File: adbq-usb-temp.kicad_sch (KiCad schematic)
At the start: 0 parts

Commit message: schem: add ESP32-S3FH4R2 symbol
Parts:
- added U1: ESP32-S3FH4R2, Package_DFN_QFN:QFN-56-1EP_7x7mm_P0.4mm_EP5.6x5.6mm, symbol PCM_Espressif:ESP32-S3
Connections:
- new net: U1.55 (VDDA), U1.56 (VDDA)
- new net GND: U1.57 (GND)
- new net VDD3P3: U1.2 (VDD3P3), U1.3 (VDD3P3)

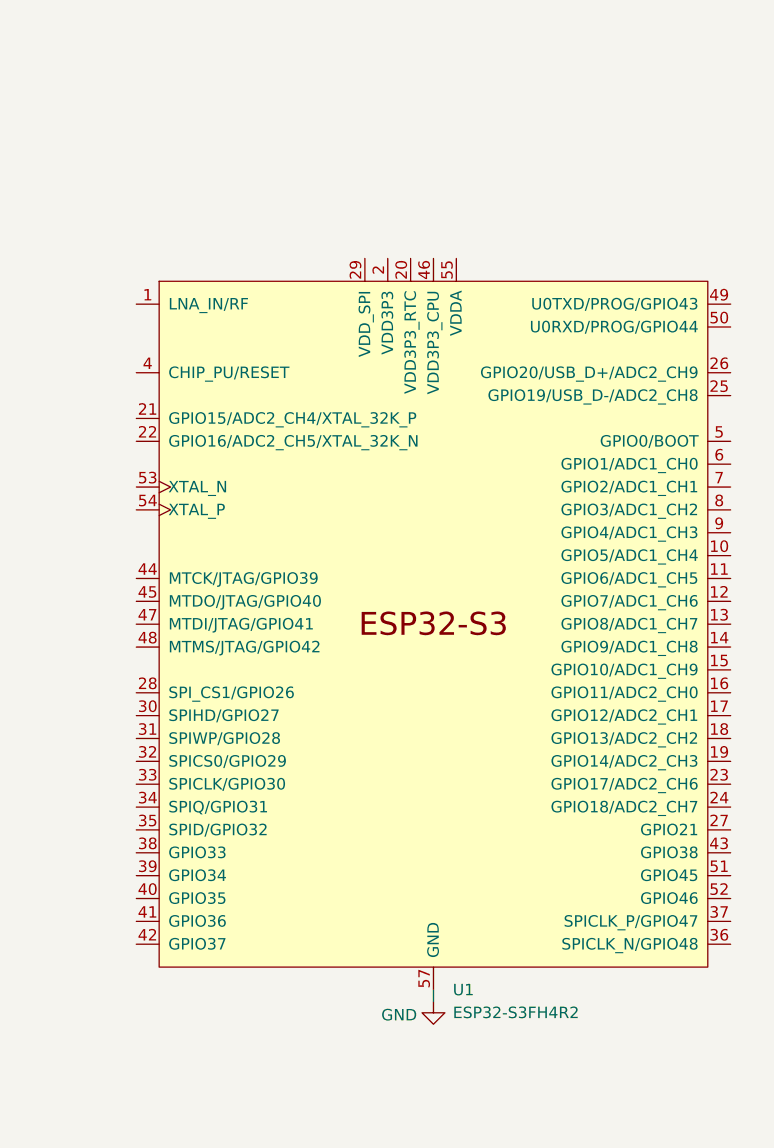
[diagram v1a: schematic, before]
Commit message: schem: add ESP32 decoupling caps
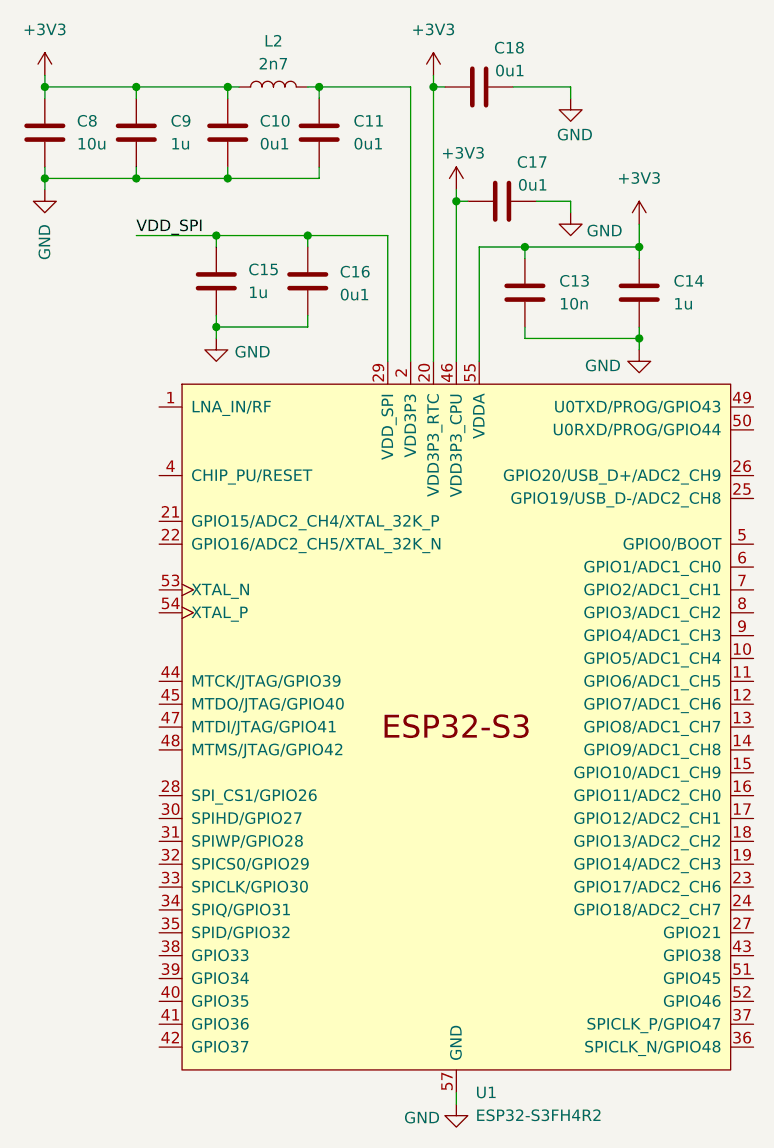
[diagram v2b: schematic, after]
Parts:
- added C10, C11, C16, C17, C18: 0u1, Capacitor_SMD:C_0402_1005Metric, symbol Device:C
- added C13: 10n, Capacitor_SMD:C_0402_1005Metric, symbol Device:C
- added C14, C15, C9: 1u, Capacitor_SMD:C_0402_1005Metric, symbol Device:C
- added C8: 10u, Capacitor_SMD:C_0402_1005Metric, symbol Device:C
- added L2: 2n7, Inductor_SMD:L_0402_1005Metric, symbol Device:L
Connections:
- net GND: now also C10.2, C11.2, C13.2, C14.2, C15.2, C16.2, C17.2, C18.2, C8.2, C9.2
- net VDD3P3: now also C11.1, L2.2
- net +3V3: now reaches U1.20 (VDD3P3_RTC)
- net +3V3: now also U1.46 (VDD3P3_CPU), U1.55 (VDDA), U1.56 (VDDA), C10.1, C13.1, C14.1, C17.1, C18.1, C8.1, C9.1, L2.1
- net VDD_SPI: now reaches U1.29 (VDD_SPI)
- net VDD_SPI: now also C15.1, C16.1
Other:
- moved on the sheet: U1

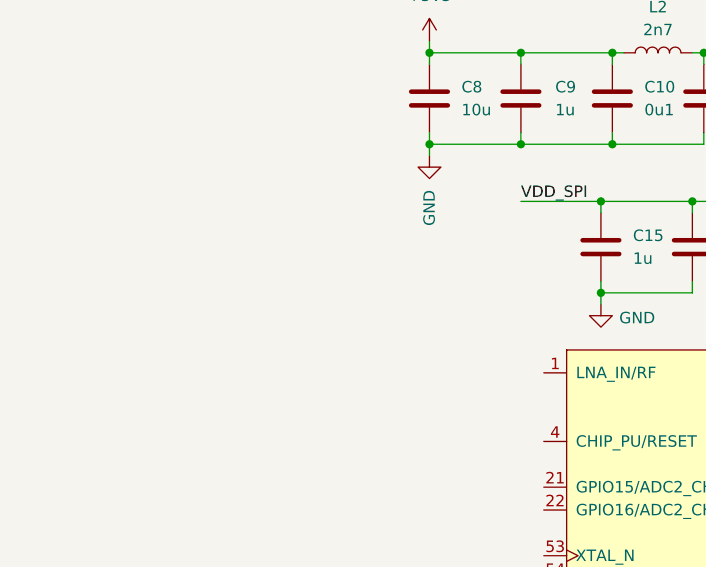
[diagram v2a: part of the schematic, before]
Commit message: schem: add rf antenna and matching networks
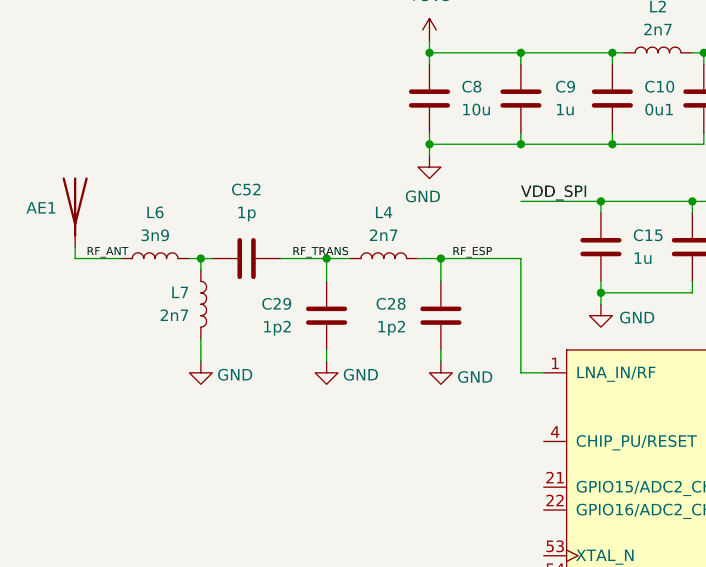
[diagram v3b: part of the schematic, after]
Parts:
- added AE1: Antenna, RF_Antenna:Johanson_2450AT18x100, symbol Device:Antenna
- added C28, C29: 1p2, Capacitor_SMD:C_0402_1005Metric, symbol Device:C
- added C52: 1p, Capacitor_SMD:C_0402_1005Metric, symbol Device:C
- added L4, L7: 2n7, Inductor_SMD:L_0402_1005Metric, symbol Device:L
- added L6: 3n9, Inductor_SMD:L_0402_1005Metric, symbol Device:L
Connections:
- net GND: now also C28.2, C29.2, L7.1
- net RF_ESP: now reaches U1.1 (LNA_IN/RF)
- net RF_ESP: now also C28.1, L4.2
- new net: C52.2, L6.2, L7.2
- new net RF_ANT: AE1.1 (A), L6.1
- new net RF_TRANS: C29.1, C52.1, L4.1

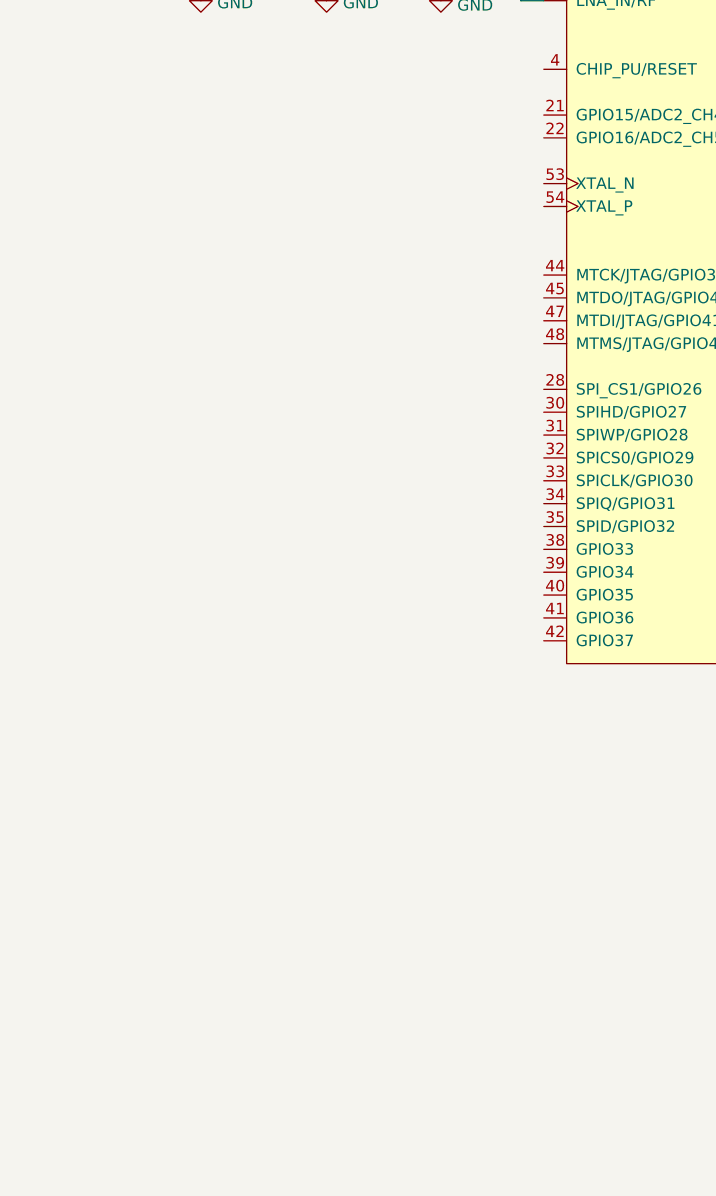
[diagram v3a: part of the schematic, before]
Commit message: schem: add HSE crystal
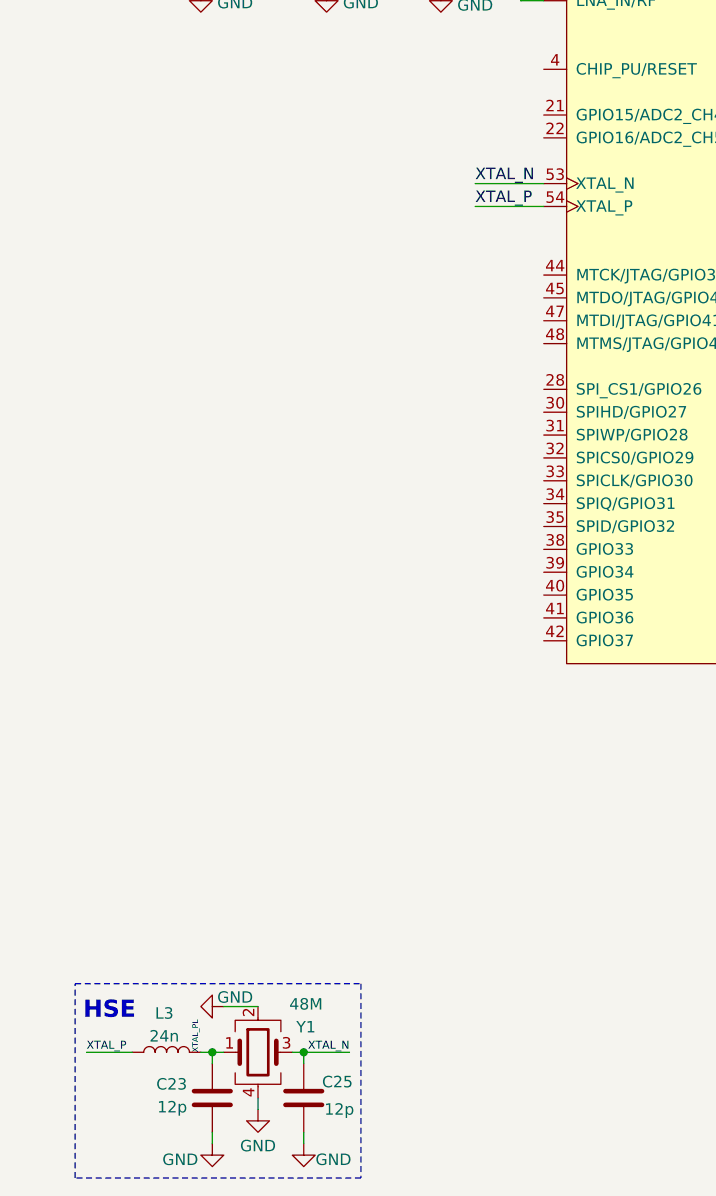
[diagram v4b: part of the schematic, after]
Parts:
- added C23, C25: 12p, Capacitor_SMD:C_0402_1005Metric, symbol Device:C
- added L3: 24n, Inductor_SMD:L_0402_1005Metric, symbol Device:L
- added Y1: 48M, Crystal:Crystal_SMD_2016-4Pin_2.0x1.6mm, symbol Device:Crystal_GND24
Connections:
- net GND: now also C23.1, C25.2, Y1.2, Y1.4
- net XTAL_N: now reaches U1.53 (XTAL_N)
- net XTAL_N: now also C25.1, Y1.3
- net XTAL_P: now reaches U1.54 (XTAL_P)
- net XTAL_P: now also L3.1
- new net XTAL_PL: C23.2, L3.2, Y1.1
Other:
- note added: "HSE"

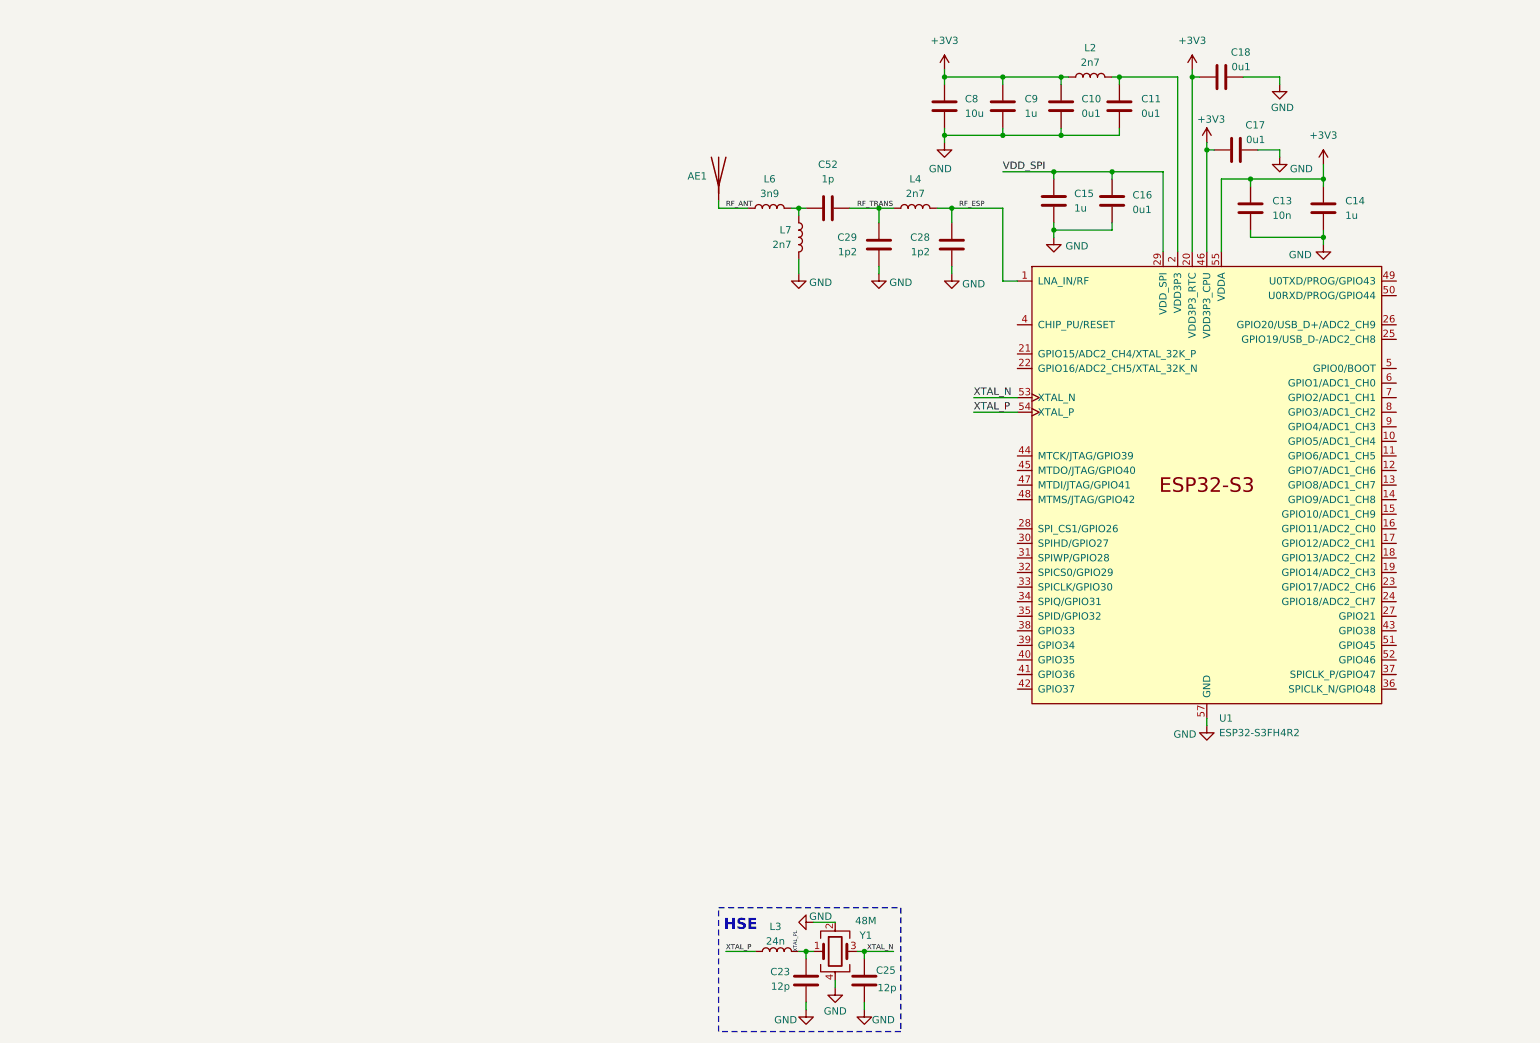
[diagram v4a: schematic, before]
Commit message: schem: add usb c connector
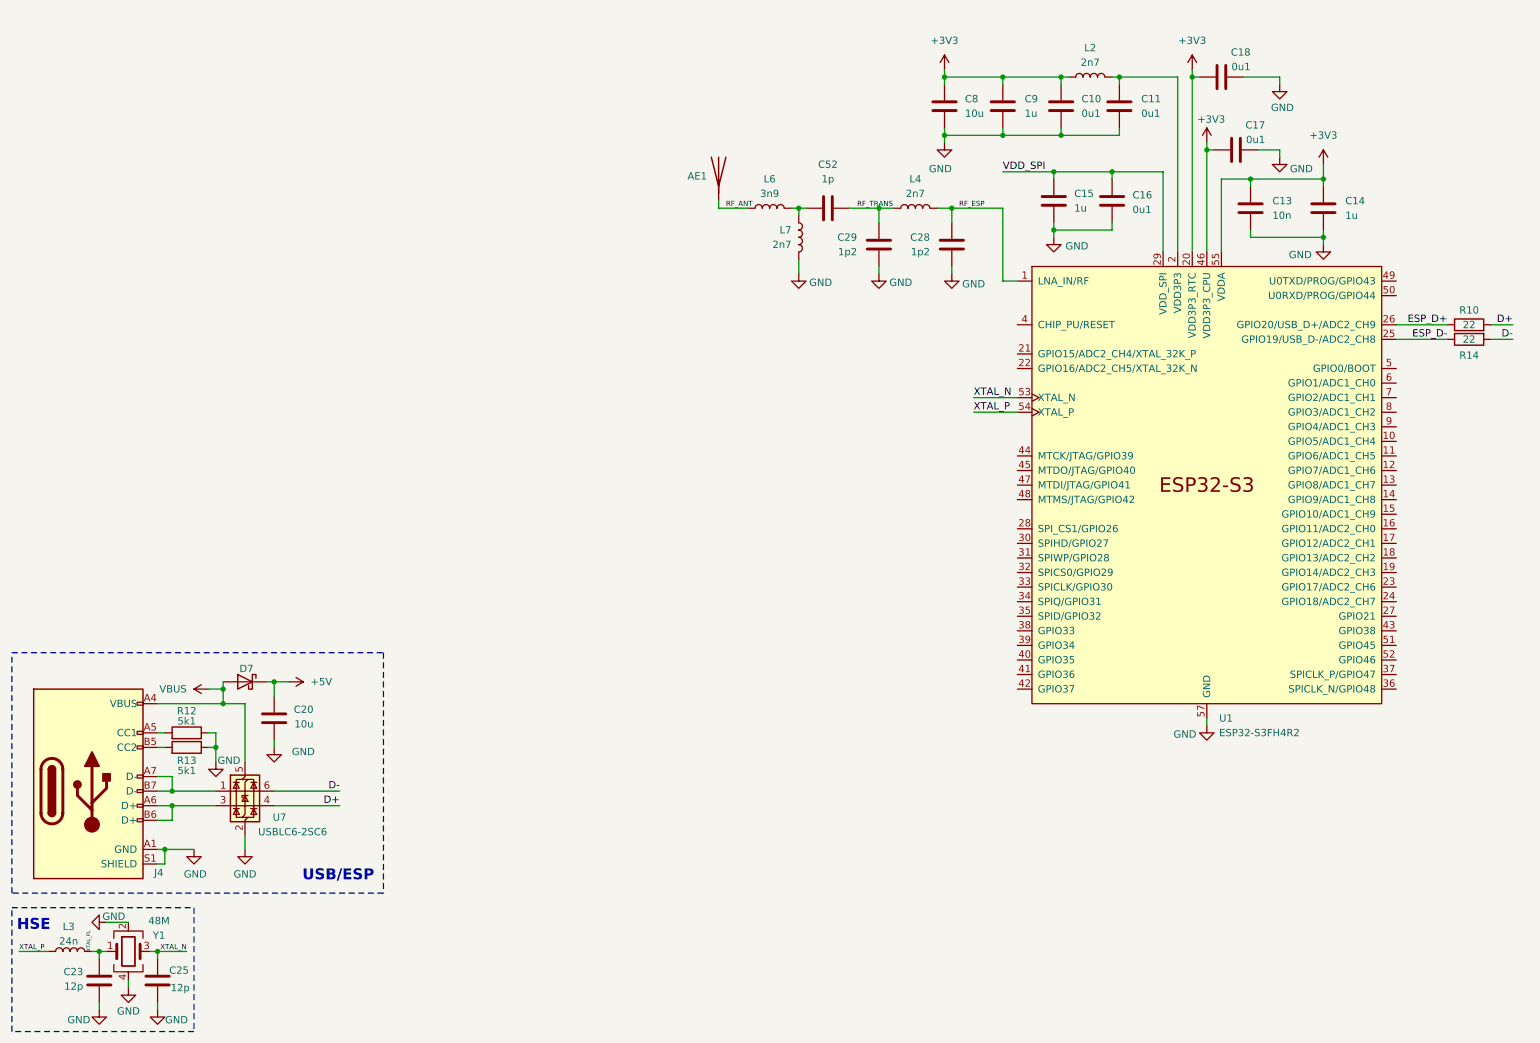
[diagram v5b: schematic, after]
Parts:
- added C20: 10u, Capacitor_SMD:C_0402_1005Metric, symbol Device:C
- added D7: D_Schottky, Diode_SMD:D_SMA, symbol Device:D_Schottky
- added J4: USB_C_Receptacle_USB2.0_14P, Connector_USB:USB_C_Receptacle_HRO_TYPE-C-31-M-12, symbol Connector:USB_C_Receptacle_USB2.0_14P
- added R10, R14: 22, Resistor_SMD:R_0402_1005Metric, symbol Device:R
- added R12, R13: 5k1, Resistor_SMD:R_0603_1608Metric, symbol Device:R
- added U7: USBLC6-2SC6, Package_TO_SOT_SMD:SOT-23-6, symbol Power_Protection:USBLC6-2SC6
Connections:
- net GND: now also C20.2, J4.A1 (GND), J4.A12 (GND), J4.B1 (GND), J4.B12 (GND), J4.S1 (SHIELD), R12.1, R13.1, U7.2 (GND)
- net ESP_D-: now reaches U1.25 (GPIO19/USB_D-/ADC2_CH8)
- net ESP_D-: now also R14.1
- net ESP_D+: now reaches U1.26 (GPIO20/USB_D+/ADC2_CH9)
- net ESP_D+: now also R10.1
- new net: J4.A5 (CC1), R12.2
- new net: J4.A6 (D+), J4.B6 (D+), U7.3 (I/O2)
- new net: J4.A7 (D-), J4.B7 (D-), U7.1 (I/O1)
- new net: J4.B5 (CC2), R13.2
- new net +5V: C20.1, D7.1 (K)
- new net D+: R10.2, U7.4 (I/O2)
- new net D-: R14.2, U7.6 (I/O1)
- new net VBUS: D7.2 (A), J4.A4 (VBUS), J4.A9 (VBUS), J4.B4 (VBUS), J4.B9 (VBUS), U7.5 (VBUS)
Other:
- note added: "USB/ESP"
- moved on the sheet: C23, C25, L3, Y1

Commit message: schem: add esp32 en pullup
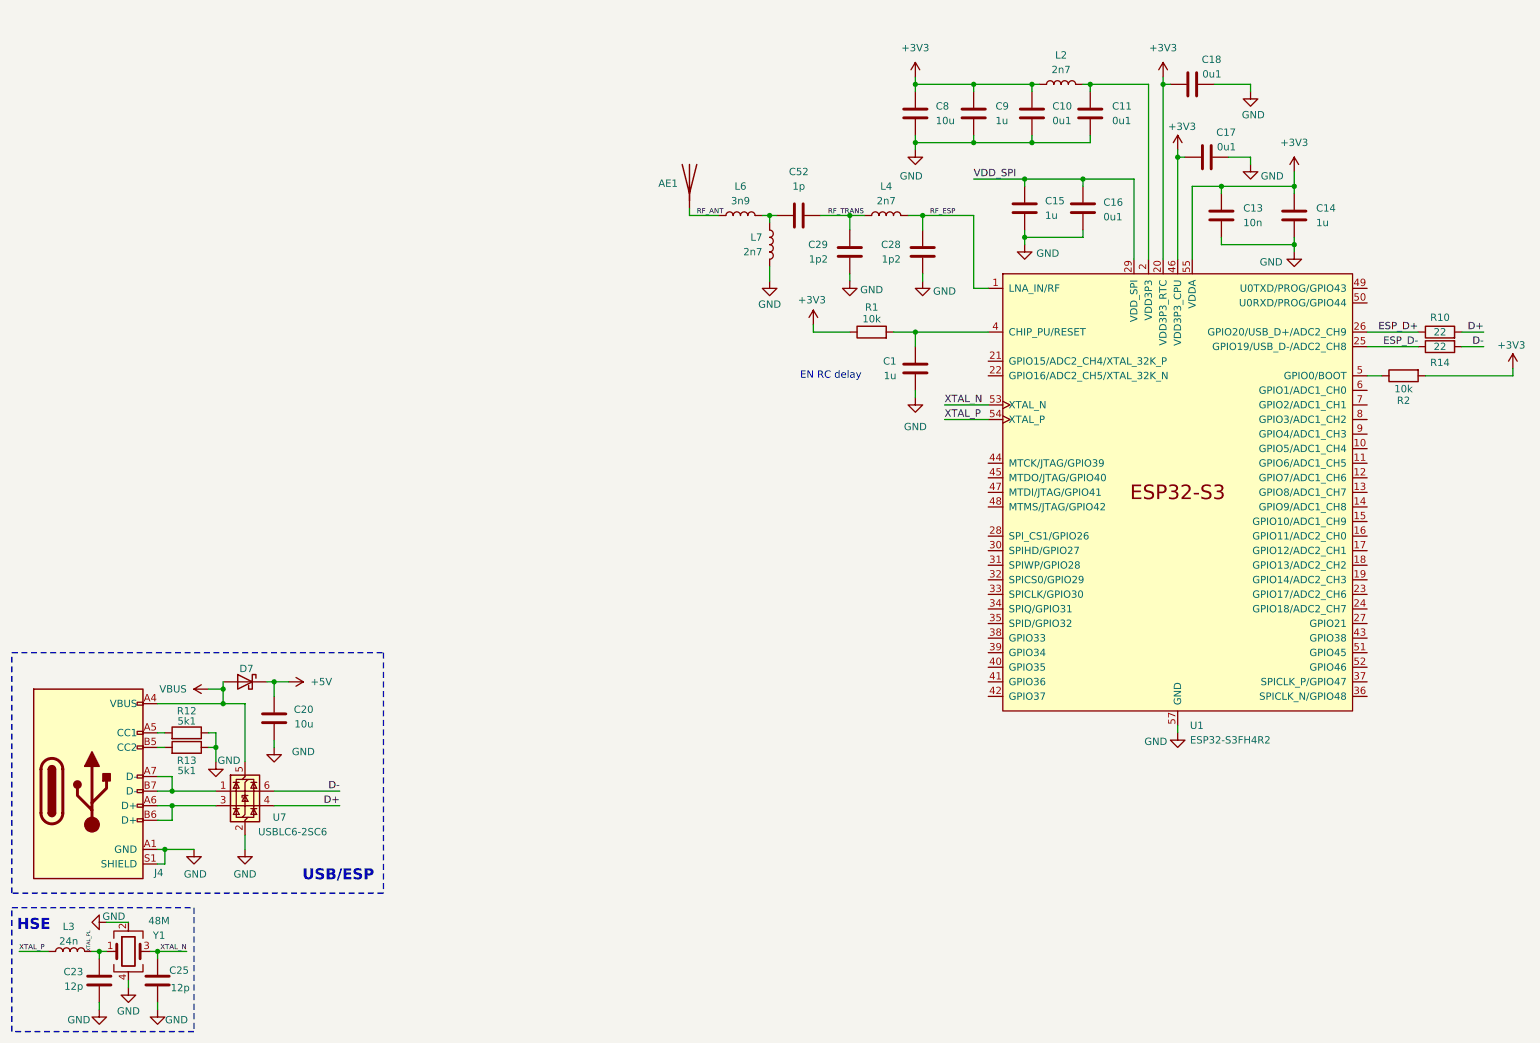
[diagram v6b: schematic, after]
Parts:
- added C1: 1u, symbol Device:C
- added R1, R2: 10k, symbol Device:R
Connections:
- net +3V3: now also R1.1, R2.2
- net GND: now also C1.2
- net at U1.4 (CHIP_PU/RESET): now also C1.1, R1.2
- net at U1.5 (GPIO0/BOOT): now also R2.1
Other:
- note added: "EN RC delay"
- moved on the sheet: AE1, C10, C11, C13, C14, C15, C16, C17, C18, C28, C29, C52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
